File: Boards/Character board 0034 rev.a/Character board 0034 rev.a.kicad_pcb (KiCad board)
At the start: 2 copper layers, 166.4 x 186.7 mm, 64 parts, among them J1 card edge, J2 character connector, Q1 2N6125, U1 2.2K, U10 Unused DIP, U11 ULN2003A, U12 ULN2003A, U13 7406, U14 74LS42, U15 LM741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

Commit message: completed 0034 rev a
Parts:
- removed C12, C7, C8: 100nF, Capacitor_THT:C_Rect_L7.0mm_W2.5mm_P5.00mm
- removed C6: 1nF, Capacitor_THT:C_Rect_L9.0mm_W2.7mm_P7.50mm_MKT
- removed R10: 47.5K, Evan's parts:R_Axial_DIN0204_L3.6mm_D1.6mm_P12.7mm_Horizontal
- removed R2, R3, R4, R5, R6: 20.0K, Evan's parts:R_Axial_DIN0204_L3.6mm_D1.6mm_P12.7mm_Horizontal
- removed R7: 120, Evan's parts:R_Axial_DIN0204_L3.6mm_D1.6mm_P12.7mm_Horizontal
- removed R8: 100K, Potentiometer_THT:Potentiometer_Bourns_3005_Horizontal
- removed R9: 10.0K, Evan's parts:R_Axial_DIN0204_L3.6mm_D1.6mm_P12.7mm_Horizontal
- removed TP6: AUD, TestPoint:TestPoint_Plated_Hole_D3.0mm
- removed U14: 74LS42, Package_DIP:DIP-16_W7.62mm
- removed U15, U9: LM741, Package_DIP:DIP-8_W7.62mm
- removed U16: AH5012, Package_DIP:DIP-16_W7.62mm
- removed U8: 3.3K, Package_DIP:DIP-16_W7.62mm
- added R12: 3.3K, Evan's parts:R_Axial_DIN0204_L3.6mm_D1.6mm_P12.7mm_Horizontal, F.Cu at (120.7, 61.0)
- added R13: 3.3K, Evan's parts:R_Axial_DIN0204_L3.6mm_D1.6mm_P12.7mm_Horizontal, F.Cu at (120.7, 63.5)
- added R14: 3.3K, Evan's parts:R_Axial_DIN0204_L3.6mm_D1.6mm_P12.7mm_Horizontal, F.Cu at (96.5, 123.8)
- added R15: 3.3K, Evan's parts:R_Axial_DIN0204_L3.6mm_D1.6mm_P12.7mm_Horizontal, F.Cu at (139.7, 61.0)
- moved F1 7.24 mm to (80.6, 123.8)
- moved C4 6.75 mm to (161.3, 41.9)
- moved C11 3.81 mm to (156.8, 96.5)
- moved R11 1.42 mm to (154.9, 93.3)
- moved C3 0.64 mm to (176.5, 46.4)
- moved U5 0.64 mm to (106.7, 127.0)
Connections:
- net 24Vpu renamed Net-(Q1-B)
- net 5Vpu renamed Net-(R13-Pad1)
- net CA2 renamed Net-(U7-CA2)
- net CS renamed Net-(U7-CS0)
- J1 pad 2: BCLK -> aux1_AGC
- J1 pad 4: UNUSED1 -> aux2_AGC
- J2 pad 2: AUD -> GND
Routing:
- net AUD: track 395.5 -> 0.00 mm, vias 2 -> 0
- net GND: track 558.6 -> 237.5 mm, vias 7 -> 3
- net Net-(R7-Pad2): track 107.3 -> 0.00 mm
- net Net-(R8-Pad1): track 101.0 -> 0.00 mm
- net Net-(U14-2): track 80.1 -> 0.00 mm
- net Net-(U14-3): track 78.2 -> 0.00 mm
- net Net-(U14-1): track 66.0 -> 0.00 mm, vias 2 -> 0
- net 24V: track 208.0 -> 143.7 mm
- net 12V: track 290.3 -> 231.5 mm, vias 3 -> 2
- net Net-(U15--): track 57.5 -> 0.00 mm
- net Net-(U14-0): track 53.2 -> 0.00 mm
- net -12V: track 260.6 -> 212.7 mm
- net Net-(U7-CS0): track 58.1 -> 20.5 mm, vias 1 -> 0
- net Net-(Q1-B): track 142.6 -> 113.6 mm, vias 3 -> 2
- net CB2: track 35.1 -> 11.7 mm
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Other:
- board text added: "07-0034 REV A"
- board text added: "SBC-2A 08-82"
- board text added: "logo goes here"
- board text removed: "ASSY 06-0004"
- board text removed: "PART 07-0004 REV B"
- board text removed: "SJC4A27-81 94V-0"

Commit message: tweaking silk
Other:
- board text added: "B"
- board text added: "C"
- board text added: "E"
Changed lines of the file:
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@@
     (property "ki_keywords" "R network parallel topology isolated")
     (attr through_hole)
-    (fp_text reference "U3" (at 9.55 6.57 180) (layer "F.SilkS")
+    (fp_text reference "U3" (at 9.525 1.905 180) (layer "F.SilkS")
         (effects (font (size 1 1) (thickness 0.15)))
     )
@@
     (property "ki_keywords" "TTL not inv OpenCol")
     (attr through_hole)
-    (fp_text reference "U13" (at 9.525 7.62 180) (layer "F.SilkS")
+    (fp_text reference "U13" (at -1.905 1.905 180) (layer "F.SilkS")
         (effects (font (size 1 1) (thickness 0.15)))
     )
@@
     (property "ki_keywords" "test point tp")
     (attr exclude_from_pos_files)
-    (fp_text reference "TP4" (at 2.54 -3.048) (layer "F.SilkS")
+    (fp_text reference "TP4" (at 4.275 -1.905) (layer "F.SilkS")
         (effects (font (size 1 1) (thickness 0.15)))
     )
-    (fp_text value "-12" (at 5.545 0) (layer "F.SilkS")
+    (fp_text value "-12" (at 4.275 0) (layer "F.SilkS")
         (effects (font (size 1 1) (thickness 0.15)))
     )
@@
     (property "ki_keywords" "R network parallel topology isolated")
     (attr through_hole)
-    (fp_text reference "U10" (at 9.525 6.985 180) (layer "F.SilkS")
+    (fp_text reference "U10" (at 9.525 1.905 180) (layer "F.SilkS")
         (effects (font (size 1 1) (thickness 0.15)))
     )
@@
     (property "ki_keywords" "test point tp")
     (attr exclude_from_pos_files)
-    (fp_text reference "TP5" (at 2.54 -3.048) (layer "F.SilkS")
+    (fp_text reference "TP5" (at 5.545 -1.905) (layer "F.SilkS")
         (effects (font (size 1 1) (thickness 0.15)))
     )
-    (fp_text value "24" (at 5.545 -1.905) (layer "F.SilkS")
+    (fp_text value "24" (at 5.545 0.635) (layer "F.SilkS")
         (effects (font (size 1 1) (thickness 0.15)))
     )
@@
     (property "ki_keywords" "test point tp")
     (attr exclude_from_pos_files)
-    (fp_text reference "TP2" (at 2.54 -3.048) (layer "F.SilkS")
+    (fp_text reference "TP2" (at 4.91 -3.048) (layer "F.SilkS")
         (effects (font (size 1 1) (thickness 0.15)))
     )
@@
     (property "ki_keywords" "connector")
     (attr through_hole)
-    (fp_text reference "U6" (at 9.525 6.35 180) (layer "F.SilkS")
+    (fp_text reference "U6" (at 9.525 1.27 180) (layer "F.SilkS")
         (effects (font (size 1 1) (thickness 0.15)))
     )
@@
     (property "ki_keywords" "cap capacitor")
     (attr through_hole)
-    (fp_text reference "C11" (at 6.985 -2.5) (layer "F.SilkS")
+    (fp_text reference "C11" (at 6.985 0 90) (layer "F.SilkS")
         (effects (font (size 1 1) (thickness 0.15)))
     )
@@
     (property "ki_keywords" "cap capacitor")
     (attr through_hole)
-    (fp_text reference "C1" (at -0.635 -3.175 -180) (layer "F.SilkS")
+    (fp_text reference "C1" (at 6.35 0 -90) (layer "F.SilkS")
         (effects (font (size 1 1) (thickness 0.15)))
     )
@@
     (property "ki_keywords" "cap capacitor")
     (attr through_hole)
-    (fp_text reference "C5" (at 6.985 2.54 90) (layer "F.SilkS")
+    (fp_text reference "C5" (at 7.54 0 90) (layer "F.SilkS")
         (effects (font (size 1 1) (thickness 0.15)))
     )
@@
     (property "ki_keywords" "connector")
     (attr through_hole)
-    (fp_text reference "J2" (at -3.41 35.985 90) (layer "F.SilkS")
+    (fp_text reference "J2" (at -3.81 42.545 90) (layer "F.SilkS")
         (effects (font (size 1 1) (thickness 0.15)))
     )
@@
     (property "ki_keywords" "test point tp")
     (attr exclude_from_pos_files)
-    (fp_text reference "TP3" (at 2.54 -3.048) (layer "F.SilkS")
+    (fp_text reference "TP3" (at 1.1 -3.175) (layer "F.SilkS")
         (effects (font (size 1 1) (thickness 0.15)))
     )
-    (fp_text value "+12" (at 3.64 1.905) (layer "F.SilkS")
+    (fp_text value "+12" (at 0.465 3.175) (layer "F.SilkS")
         (effects (font (size 1 1) (thickness 0.15)))
     )
@@
     (property "ki_keywords" "PIA")
     (attr through_hole)
-    (fp_text reference "U7" (at 17.78 22.86 180) (layer "F.SilkS")
+    (fp_text reference "U7" (at 7.62 -4.445 180) (layer "F.SilkS")
         (effects (font (size 1 1) (thickness 0.15)))
     )
@@
     (property "ki_keywords" "R network parallel topology isolated")
     (attr through_hole)
-    (fp_text reference "U4" (at 9.525 6.35 180) (layer "F.SilkS")
+    (fp_text reference "U4" (at 9.525 1.905 180) (layer "F.SilkS")
         (effects (font (size 1 1) (thickness 0.15)))
     )
@@
     (property "ki_keywords" "darlington transistor array")
     (attr through_hole)
-    (fp_text reference "U12" (at 9.525 6.35 180) (layer "F.SilkS")
+    (fp_text reference "U12" (at 9.525 2.54 180) (layer "F.SilkS")
         (effects (font (size 1 1) (thickness 0.15)))
     )
@@
     (property "ki_keywords" "fuse")
     (attr through_hole)
-    (fp_text reference "F1" (at -3.175 -4.445 unlocked) (layer "F.SilkS")
+    (fp_text reference "F1" (at 15.875 10.795 unlocked) (layer "F.SilkS")
         (effects (font (size 1 1) (thickness 0.15)))
     )
@@
     (property "ki_keywords" "cap capacitor")
     (attr through_hole)
-    (fp_text reference "C2" (at 0.635 -3.81 180) (layer "F.SilkS")
+    (fp_text reference "C2" (at 0.635 -3.81 270) (layer "F.SilkS")
         (effects (font (size 1 1) (thickness 0.15)))
     )
@@
     (property "ki_keywords" "test point tp")
     (attr exclude_from_pos_files)
-    (fp_text reference "TP1" (at 2.54 -3.048) (layer "F.SilkS")
+    (fp_text reference "TP1" (at 4.91 -2.54) (layer "F.SilkS")
         (effects (font (size 1 1) (thickness 0.15)))
     )
@@
     (property "ki_keywords" "R network parallel topology isolated")
     (attr through_hole)
-    (fp_text reference "U5" (at 9.525 6.35 180) (layer "F.SilkS")
+    (fp_text reference "U5" (at 9.525 2.54 180) (layer "F.SilkS")
         (effects (font (size 1 1) (thickness 0.15)))
     )
@@
     (property "ki_keywords" "R network parallel topology isolated")
     (attr through_hole)
-    (fp_text reference "U1" (at 9.525 4.445 180) (layer "F.SilkS")
+    (fp_text reference "U1" (at 9.525 7.45 180) (layer "F.SilkS")
         (effects (font (size 1 1) (thickness 0.15)))
     )
@@
     (property "ki_keywords" "PNP Transistor")
     (attr through_hole)
-    (fp_text reference "Q1" (at 10.16 -8.8) (layer "F.SilkS")
+    (fp_text reference "Q1" (at -5.08 -8.89) (layer "F.SilkS")
         (effects (font (size 1 1) (thickness 0.15)))
     )
@@
     (property "ki_keywords" "darlington transistor array")
     (attr through_hole)
-    (fp_text reference "U11" (at 9.525 6.985 180) (layer "F.SilkS")
+    (fp_text reference "U11" (at 9.525 3.175 180) (layer "F.SilkS")
         (effects (font (size 1 1) (thickness 0.15)))
     )
@@
     (effects (font (size 1.5 1.5) (thickness 0.3) bold) (justify left bottom mirror))
   )
+  (gr_text "E" (at 85.725 114.3) (layer "F.SilkS")
+    (effects (font (size 1 1) (thickness 0.15)) (justify left bottom))
+  )
+  (gr_text "C" (at 80.01 120.65) (layer "F.SilkS")
+    (effects (font (size 1 1) (thickness 0.15)) (justify left bottom))
+  )
+  (gr_text "B" (at 74.93 114.3) (layer "F.SilkS")
+    (effects (font (size 1 1) (thickness 0.15)) (justify left bottom))
+  )
   (segment (start 147.32 63.5) (end 149.86 60.96) (width 0.4) (layer "F.Cu") (net 84))
   (segment (start 152.4 73.66) (end 152.4 73.025) (width 0.4) (layer "F.Cu") (net 84))
@@
         (xy 184.785 20.955)
         (xy 182.88 20.955)
-        (xy 182.88 20.955)
         (xy 74.93 20.955)
         (xy 62.865 32.385)
@@
       (pts
         (xy 71.755 113.03)
-        (xy 71.755 131.445)
-        (xy 75.565 135.255)
+        (xy 71.755 130.175)
+        (xy 75.565 133.985)
         (xy 75.565 158.75)
         (xy 85.725 158.75)
@@
         (xy 168.275 113.03)
         (xy 168.275 119.38)
-        (xy 168.275 119.38)
         (xy 168.275 164.465)

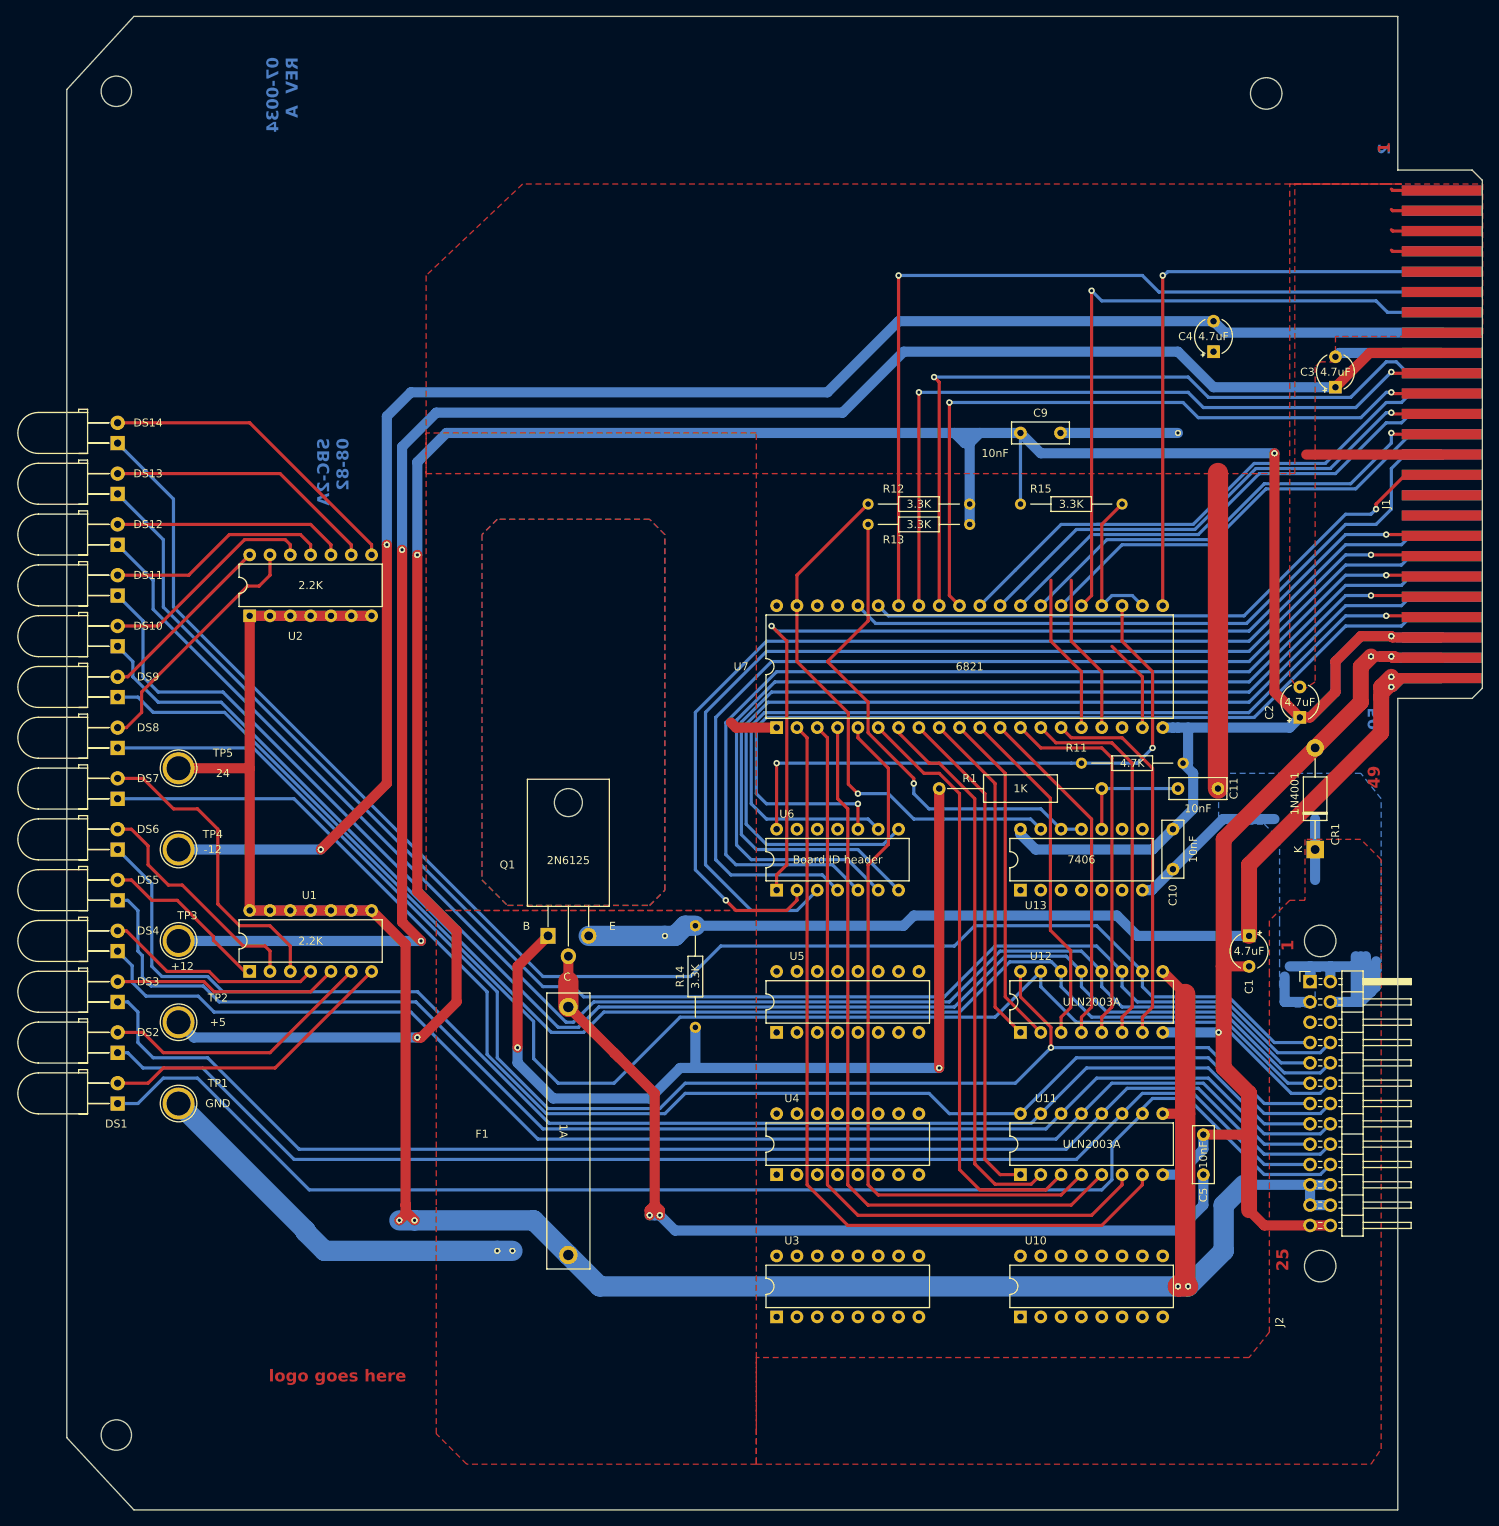
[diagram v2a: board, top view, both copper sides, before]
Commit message: revised 0034 rev a led spacing and fuse length
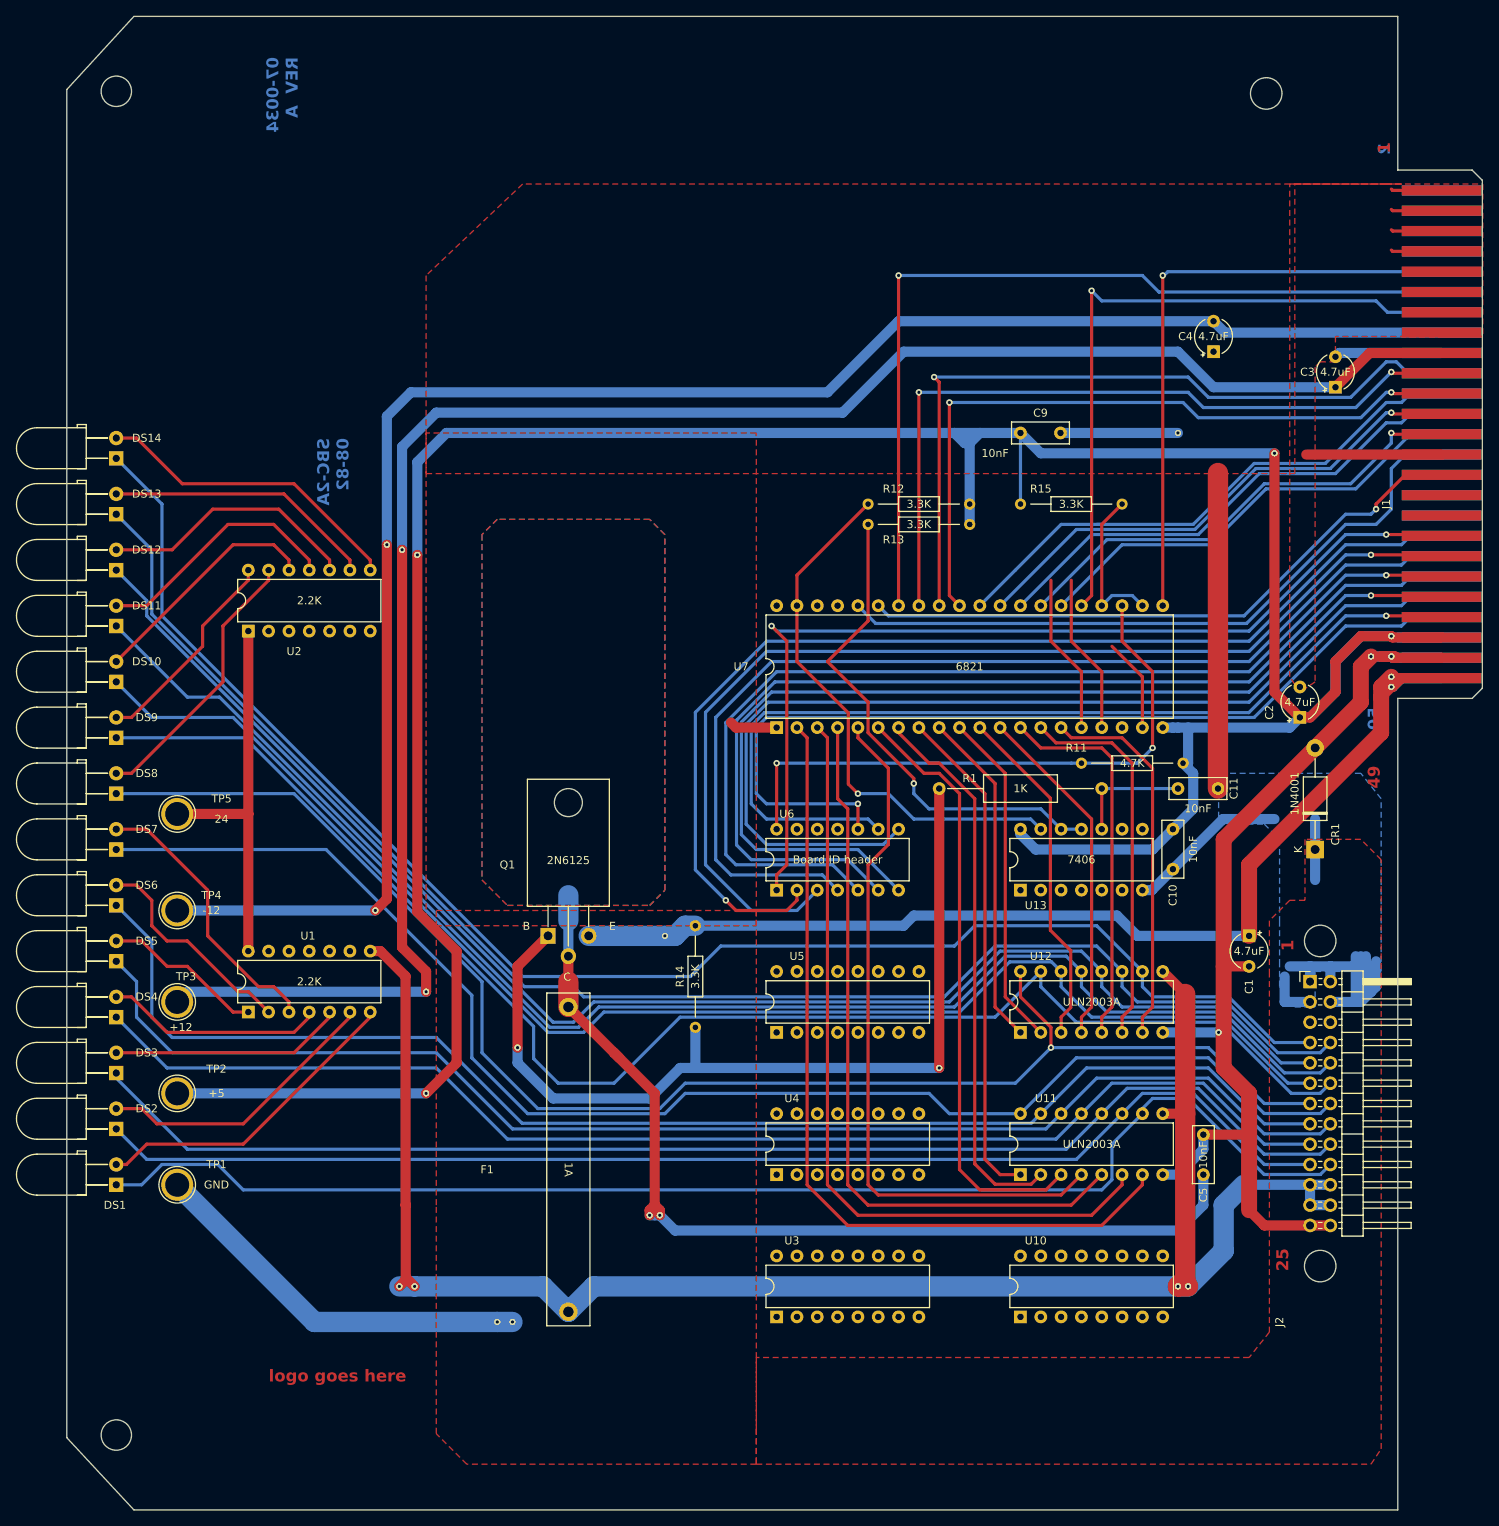
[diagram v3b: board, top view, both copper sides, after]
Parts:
- moved TP1 10.2 mm to (31.8, 146.1)
- moved DS1 10.2 mm to (24.1, 143.5)
- moved DS2 9.53 mm to (24.1, 136.5)
- moved TP2 8.89 mm to (31.8, 134.6)
- moved DS3 8.89 mm to (24.1, 129.5)
- moved DS4 8.26 mm to (24.1, 122.6)
- moved TP3 7.62 mm to (31.8, 123.2)
- moved TP4 7.62 mm to (31.8, 111.8)
- moved DS5 7.62 mm to (24.1, 115.6)
- moved DS6 6.99 mm to (24.1, 108.6)
- moved DS7 6.35 mm to (24.1, 101.6)
- moved DS8 5.72 mm to (24.1, 94.6)
- moved TP5 5.72 mm to (31.8, 99.7)
- moved DS9 5.08 mm to (24.1, 87.6)
- moved U1 5.08 mm to (40.6, 124.5)
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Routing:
- net 24Vout: track 320.7 -> 273.0 mm
- net -12V: track 212.7 -> 224.5 mm
- net 12V: track 231.5 -> 239.5 mm
- net Net-(Q1-C): track 114.7 -> 122.3 mm
- net 5V: track 375.3 -> 382.0 mm
- net B2out: track 189.4 -> 183.9 mm
- net A2out: track 168.5 -> 163.2 mm
- net A4out: track 174.0 -> 169.1 mm
- net A0out: track 170.9 -> 166.3 mm
- net A3out: track 166.1 -> 161.6 mm
- net A1out: track 161.7 -> 157.9 mm
- net Net-(DS7-A): track 38.9 -> 35.2 mm
- net Net-(DS12-A): track 29.0 -> 32.7 mm
- net Net-(DS9-A): track 22.8 -> 26.4 mm
- net Net-(DS8-A): track 31.0 -> 34.4 mm
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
